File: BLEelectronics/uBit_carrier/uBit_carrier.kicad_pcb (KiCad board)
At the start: 2 copper layers, 57.8 x 32.1 mm, 7 parts, among them J1 microbit_edge_connector, J2 Conn_01x02_Male, U1 W25Q32JVSS, U2 XC6206PxxxMR

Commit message: Progress as of 3:30 PM MDT... Passing off to Matt
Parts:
- added J3: Micro_SD_Card_Det_Hirose_DM3AT, Connector_Card:microSD_HC_Hirose_DM3AT-SF-PEJM5, F.Cu at (191.6, 105.2)
- U1: value W25Q32JVSS -> W25Q128JV
- U2: value XC6206PxxxMR -> XC6206P332MR
- moved C3 16.8 mm to (175.8, 104.4), turned to 0 degrees

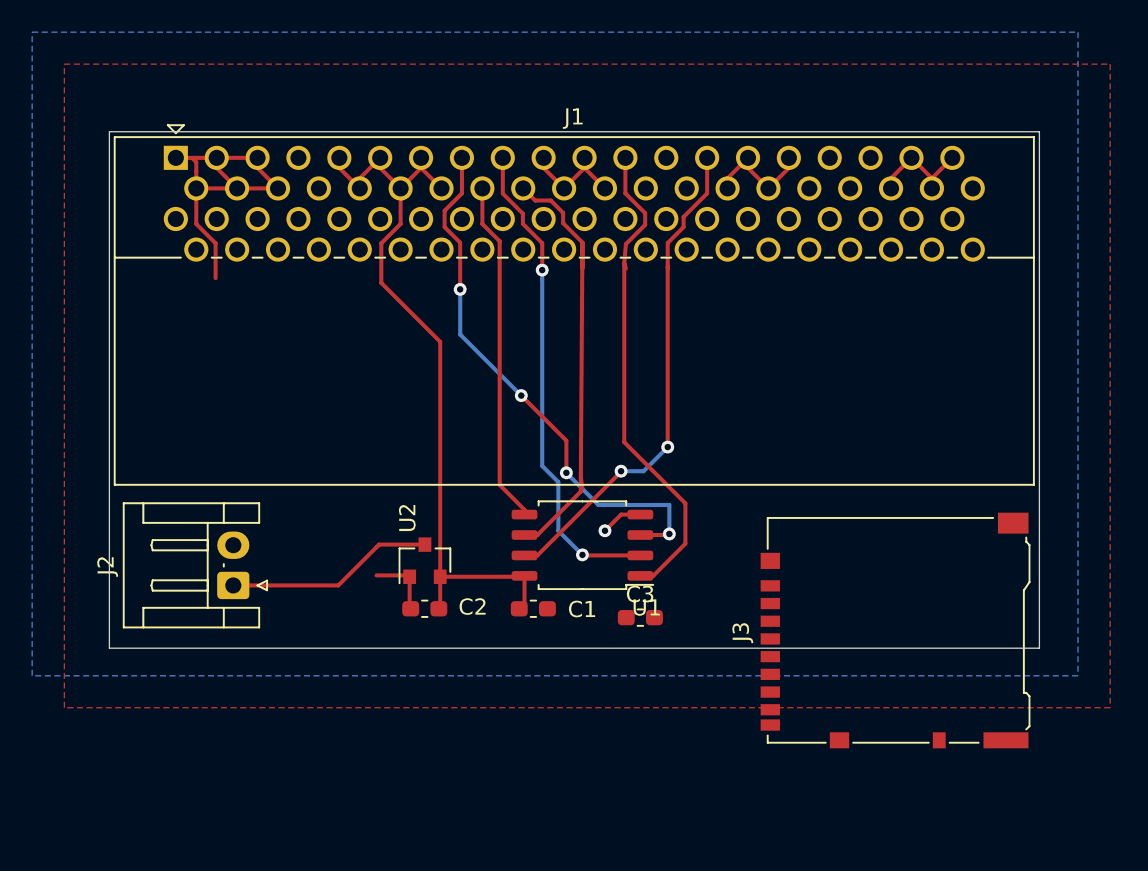
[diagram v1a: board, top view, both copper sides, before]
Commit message: Full sch and layout of uBit carrier.
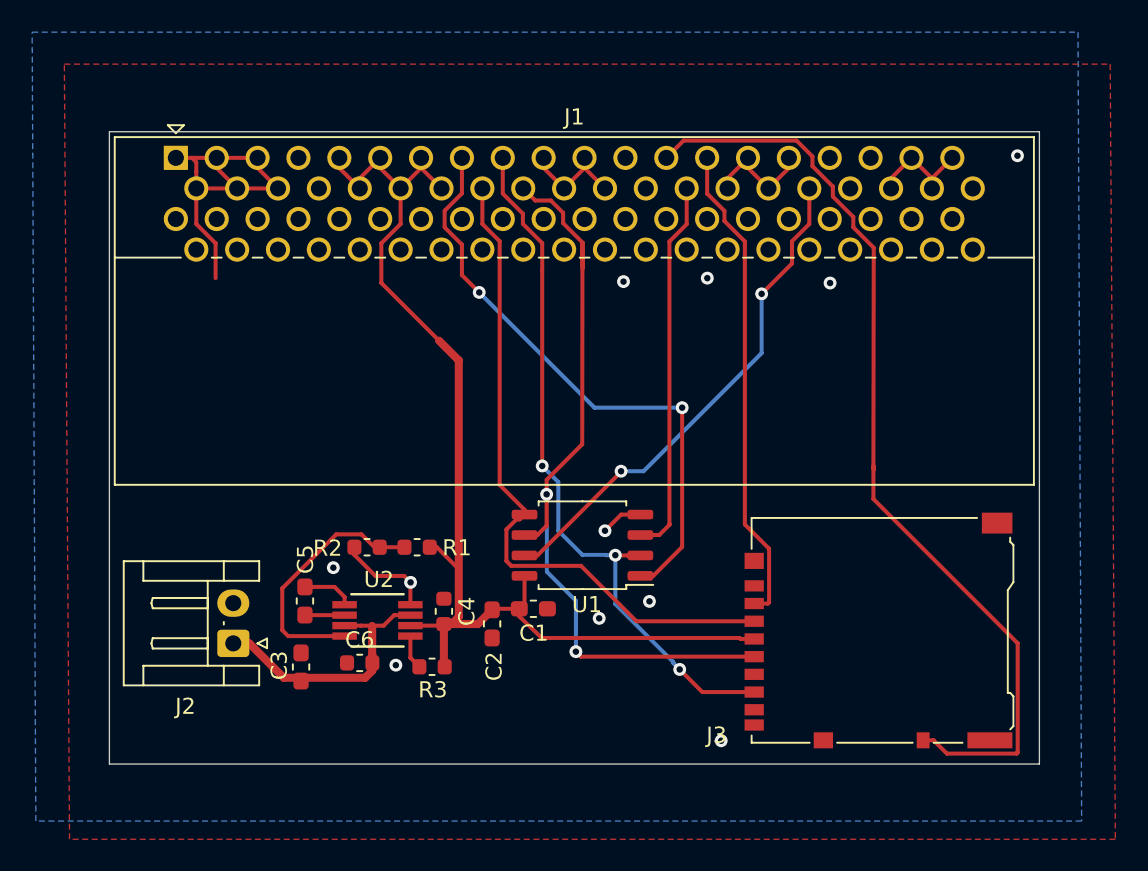
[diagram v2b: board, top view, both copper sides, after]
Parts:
- added C4: 10uF, Capacitor_SMD:C_0603_1608Metric, F.Cu at (163.6, 104.0)
- added C5: 1uF, Capacitor_SMD:C_0603_1608Metric_Pad1.05x0.95mm_HandSolder, F.Cu at (155.0, 103.4)
- added C6: 10uF, Capacitor_SMD:C_0603_1608Metric, F.Cu at (158.4, 107.2)
- added R1: 17K3, Resistor_SMD:R_0603_1608Metric, F.Cu at (161.9, 100.0)
- added R2: 10K, Resistor_SMD:R_0603_1608Metric, F.Cu at (158.8, 100.0)
- added R3: 100K, Resistor_SMD:R_0603_1608Metric, F.Cu at (162.9, 107.5)
- U2: value XC6206P332MR -> MCP1253-ADJI_MS; footprint Package_TO_SOT_SMD:SOT-23 -> 0my_footprints:MCP1253-ADJI_MS
- moved C3 21.3 mm to (154.7, 107.5), turned to 270 degrees
- moved U2 4.74 mm to (159.5, 104.6), turned to 180 degrees
- moved C2 4.29 mm to (166.6, 104.8), turned to 90 degrees
- moved J2 3.60 mm to (150.5, 106.0)
- moved J3 1.00 mm to (190.6, 105.2)
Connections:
- C3 pad 2: Net-(C3-Pad2) -> /VIN
- J1 pad 10: (no net) -> Net-(J1-Pad10)
- J1 pad 12: (no net) -> Net-(J1-Pad12)
- J1 pad 13: (no net) -> Net-(J1-Pad13)
- J1 pad 14: (no net) -> Net-(J1-Pad14)
- J1 pad 15: (no net) -> Net-(J1-Pad15)
- J1 pad 16: (no net) -> Net-(J1-Pad16)
- J1 pad 18: (no net) -> Net-(J1-Pad18)
- J1 pad 2: (no net) -> Net-(J1-Pad2)
- J1 pad 20: (no net) -> Net-(J1-Pad20)
- J1 pad 22: (no net) -> Net-(J1-Pad22)
- J1 pad 24: (no net) -> Net-(J1-Pad24)
- J1 pad 26: (no net) -> Net-(J1-Pad26)
- J1 pad 28: (no net) -> Net-(J1-Pad28)
- J1 pad 29: /wp -> /~CS0
- J1 pad 30: (no net) -> Net-(J1-Pad30)
- J1 pad 32: (no net) -> Net-(J1-Pad32)
- J1 pad 34: (no net) -> Net-(J1-Pad34)
- J1 pad 36: (no net) -> Net-(J1-Pad36)
- J1 pad 38: (no net) -> Net-(J1-Pad38)
- J1 pad 4: (no net) -> Net-(J1-Pad4)
- J1 pad 40: (no net) -> Net-(J1-Pad40)
- J1 pad 42: (no net) -> Net-(J1-Pad42)
- J1 pad 44: (no net) -> Net-(J1-Pad44)
- J1 pad 45: /~CS -> Net-(J1-Pad45)
- J1 pad 46: (no net) -> Net-(J1-Pad46)
- J1 pad 47: (no net) -> Net-(J1-Pad47)
- J1 pad 48: (no net) -> Net-(J1-Pad48)
- J1 pad 49: (no net) -> /CD
- J1 pad 50: (no net) -> Net-(J1-Pad50)
- J1 pad 51: (no net) -> /wp
- J1 pad 52: (no net) -> Net-(J1-Pad52)
- J1 pad 53: /hold -> /~CS1
- J1 pad 54: (no net) -> Net-(J1-Pad54)
- J1 pad 56: (no net) -> Net-(J1-Pad56)
- J1 pad 58: (no net) -> Net-(J1-Pad58)
- J1 pad 6: (no net) -> Net-(J1-Pad6)
- J1 pad 60: (no net) -> Net-(J1-Pad60)
- J1 pad 62: (no net) -> Net-(J1-Pad62)
- J1 pad 63: (no net) -> /hold
- J1 pad 64: (no net) -> Net-(J1-Pad64)
- J1 pad 65: (no net) -> Net-(J1-Pad65)
- J1 pad 66: (no net) -> Net-(J1-Pad66)
- J1 pad 67: (no net) -> Net-(J1-Pad67)
- J1 pad 68: (no net) -> Net-(J1-Pad68)
- J1 pad 69: (no net) -> Net-(J1-Pad69)
- J1 pad 70: (no net) -> Net-(J1-Pad70)
- J1 pad 72: (no net) -> Net-(J1-Pad72)
- J1 pad 74: (no net) -> Net-(J1-Pad74)
- J1 pad 76: (no net) -> Net-(J1-Pad76)
- J1 pad 78: (no net) -> Net-(J1-Pad78)
- J1 pad 79: (no net) -> Net-(J1-Pad79)
- J1 pad 8: (no net) -> Net-(J1-Pad8)
- J1 pad 80: (no net) -> Net-(J1-Pad80)
- J2 pad 1: Net-(C3-Pad2) -> /VIN
- J3 pad 1: (no net) -> Net-(J3-Pad1)
- J3 pad 10: (no net) -> /CD
- J3 pad 11: Net-(J3-Pad11) -> GND
- J3 pad 2: (no net) -> /~CS1
- J3 pad 3: (no net) -> /mosi
- J3 pad 4: (no net) -> /3.3V
- J3 pad 5: (no net) -> /sclk
- J3 pad 6: (no net) -> GND
- J3 pad 7: (no net) -> /miso
- J3 pad 8: (no net) -> Net-(J3-Pad8)
- J3 pad 9: (no net) -> Net-(J3-Pad9)
- U1 pad 1: /~CS -> /~CS0
- U2 pad 1: GND -> Net-(R3-Pad1)
- U2 pad 3: Net-(C3-Pad2) -> /VIN
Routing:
- net /CD: track 0.00 -> 58.7 mm
- net /~CS0: track 0.00 -> 37.3 mm, vias 0 -> 2
- net /~CS: track 30.5 -> 0.00 mm
- net /~CS1: track 0.00 -> 30.2 mm
- net /3.3V: track 47.1 -> 71.9 mm
- net /sclk: track 27.8 -> 48.9 mm, vias 0 -> 2
- net /mosi: track 21.4 -> 41.8 mm
- net /VIN: track 0.00 -> 16.9 mm
- net Net-(R1-Pad1): track 0.00 -> 15.9 mm
- net /miso: track 30.3 -> 45.1 mm, vias 2 -> 3
- net Net-(C3-Pad2): track 13.0 -> 0.00 mm
- net /wp: track 34.1 -> 23.4 mm, vias 4 -> 0
- net Net-(C5-Pad1): track 0.00 -> 3.20 mm
- net Net-(C5-Pad2): track 0.00 -> 2.47 mm
- net Net-(R3-Pad1): track 0.00 -> 2.14 mm
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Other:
- board size 57.8 x 32.1 mm -> 57.8 x 39.3 mm

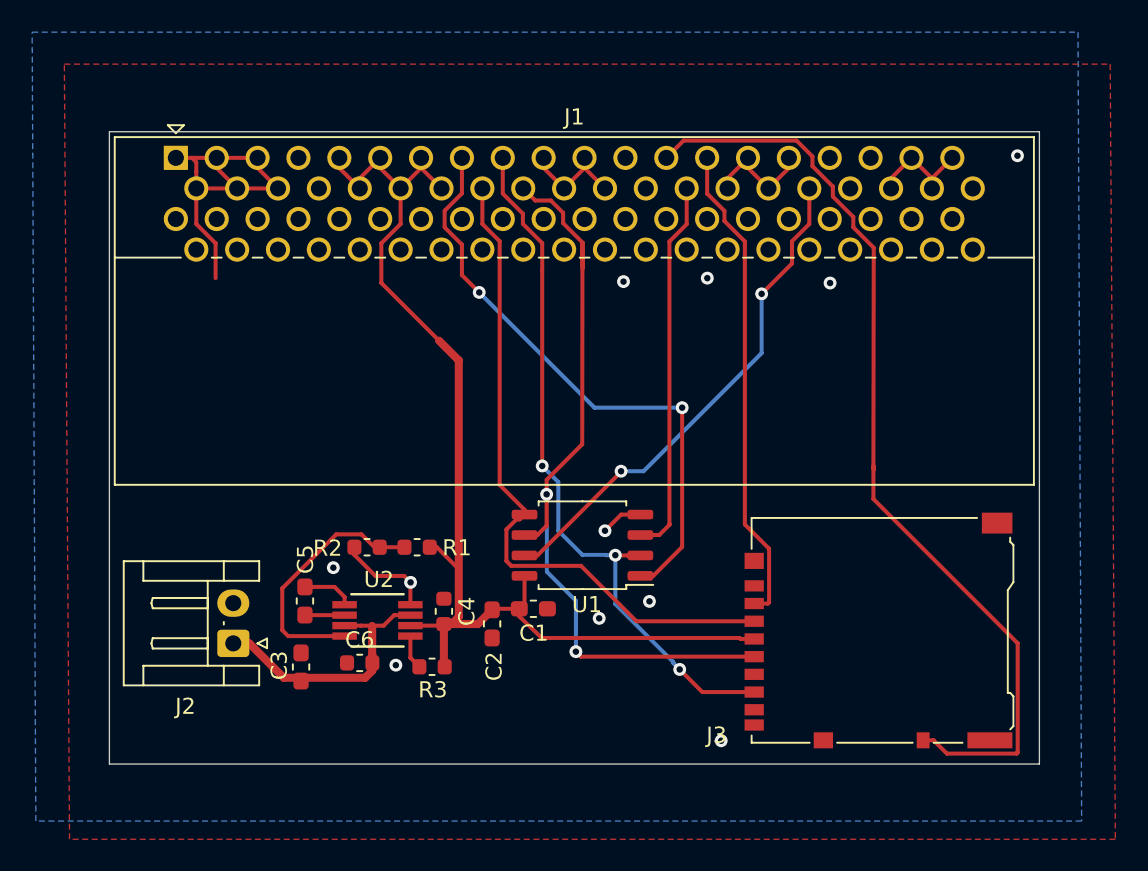
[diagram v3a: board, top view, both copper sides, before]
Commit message: BOM clean, pdf generated, rev0 submitted to JLCPCB
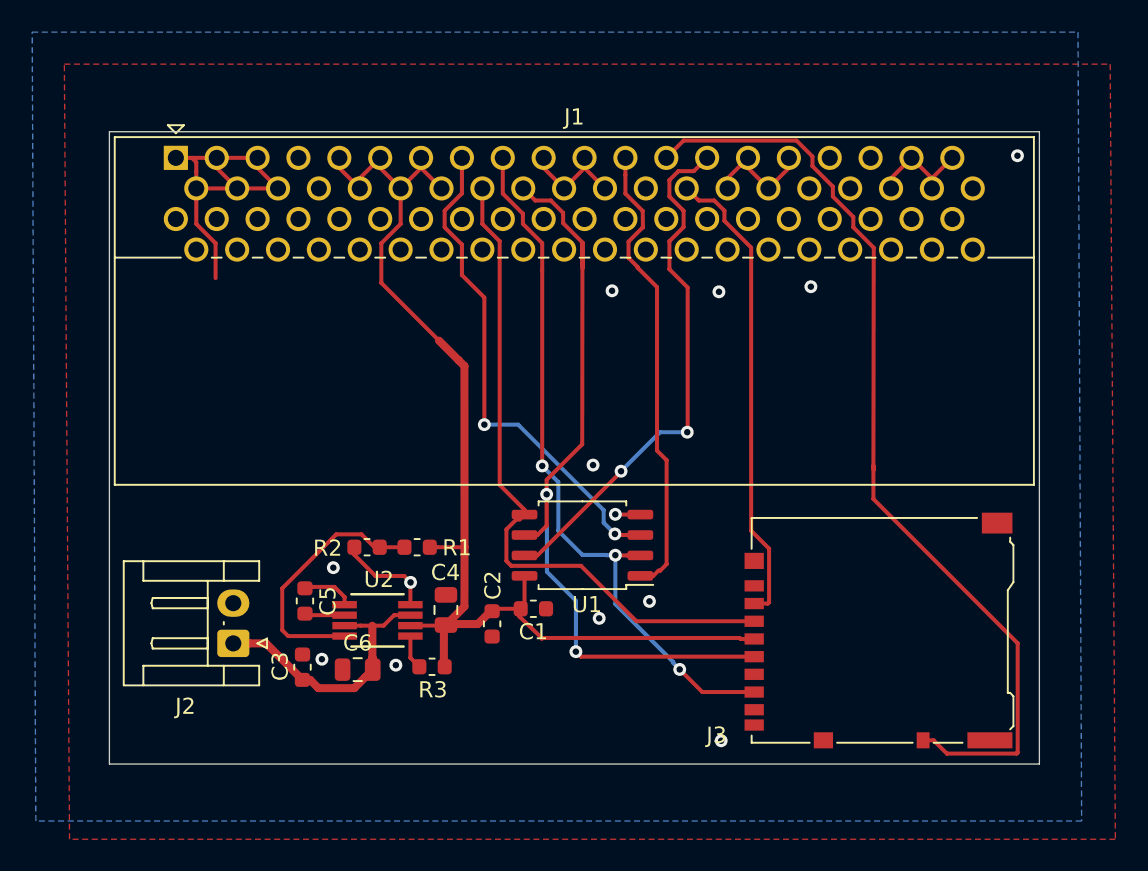
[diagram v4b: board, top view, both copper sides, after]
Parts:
- C1: value 0.1uF -> 100nF; footprint Capacitor_SMD:C_0603_1608Metric_Pad1.05x0.95mm_HandSolder -> Capacitor_SMD:C_0603_1608Metric
- C2, C3, C5: footprint Capacitor_SMD:C_0603_1608Metric_Pad1.05x0.95mm_HandSolder -> Capacitor_SMD:C_0603_1608Metric
- C4, C6: footprint Capacitor_SMD:C_0603_1608Metric -> Capacitor_SMD:C_0805_2012Metric
- R1: value 17K3 -> 17K4
- moved C6 0.44 mm to (158.2, 107.6)
- moved C4 0.16 mm to (163.7, 103.9)
- moved C3 0.09 mm to (154.8, 107.5)
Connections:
- C4 pad 1: Net-(C4-Pad1) -> GND
- J1 pad 29: /~CS0 -> /wp
- J1 pad 45: Net-(J1-Pad45) -> /~CS0
- J1 pad 51: /wp -> /~CS1
- J1 pad 53: /~CS1 -> /hold
- J1 pad 63: /hold -> Net-(J1-Pad63)
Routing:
- net /~CS0: track 37.3 -> 29.0 mm, vias 2 -> 0
- net /wp: track 23.4 -> 31.0 mm, vias 0 -> 2
- net /VIN: track 16.9 -> 18.9 mm
- net /hold: track 31.4 -> 33.1 mm
- net GND: track 31.8 -> 30.7 mm, vias 11 -> 13
- net /3.3V: track 71.9 -> 72.8 mm
- net /~CS1: track 30.2 -> 29.4 mm
